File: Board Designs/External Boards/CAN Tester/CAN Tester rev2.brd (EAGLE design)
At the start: 83.8 x 100.3 mm, 30 parts, among them M1 Minifit-1, M2 Nanofit-1, M3 Nanofit-2, M4 Minifit-2, U1 ISOLATED CAN TRANSCIEVER, U3 TEENSY_3.2_SIMPLE, U4 CHARACTER_LCD

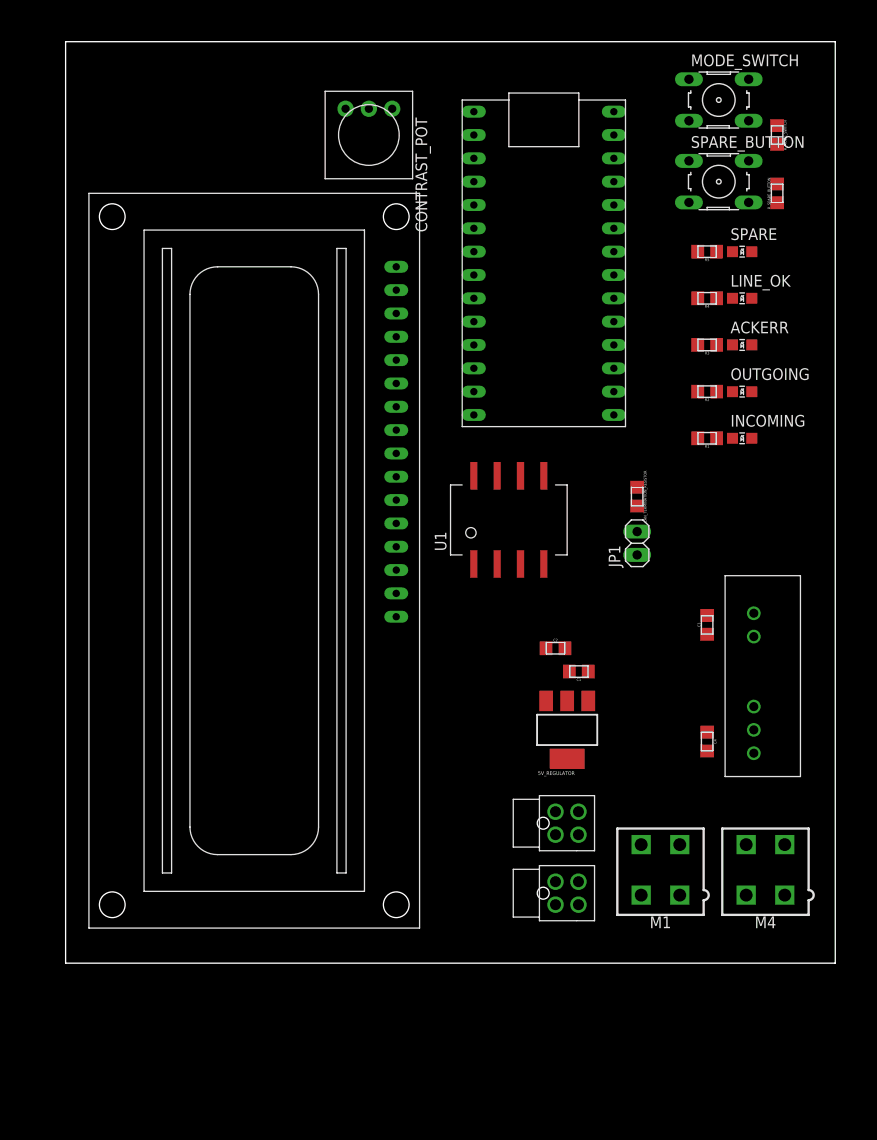
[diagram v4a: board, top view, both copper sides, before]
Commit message: Adjusted schematic to make the connections clearer for CAN_Tester, and verified it
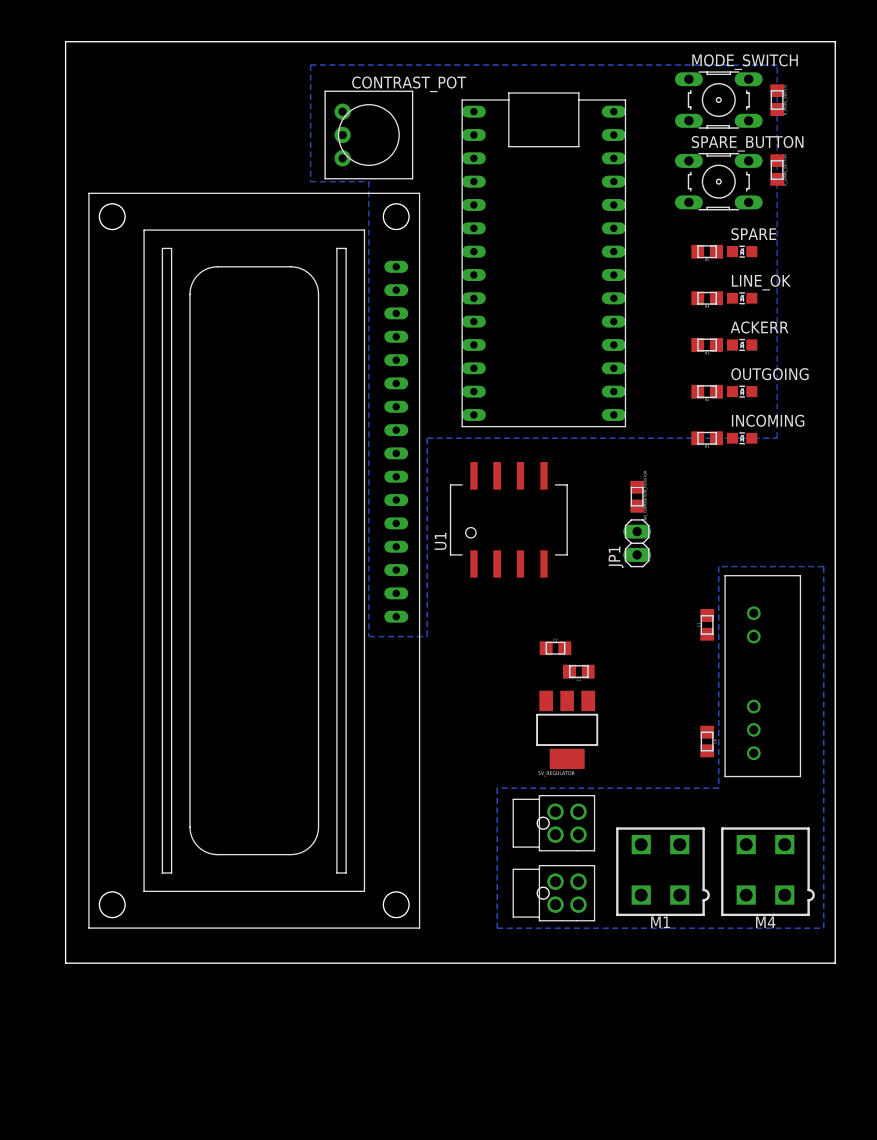
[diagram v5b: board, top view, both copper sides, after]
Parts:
- moved R_MODE_SWITCH 3.81 mm to (77.5, 92.7)
- moved R_SPARE_BUTTON 2.54 mm to (77.5, 85.1), turned to 270 degrees
- turned CONTRAST_POT to 270 degrees
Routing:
- added copper zone on layer 16, net GND
- added copper zone on layer 16, net GND_ISOLATED
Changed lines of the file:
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@@
 <param name="TopRouterVariant" value="1"/>
 <param name="tpViaShape" value="round"/>
-<param name="PrefDir.1" value="0"/>
+<param name="PrefDir.1" value="a"/>
 <param name="PrefDir.2" value="0"/>
 <param name="PrefDir.3" value="0"/>
@@
 <param name="PrefDir.14" value="0"/>
 <param name="PrefDir.15" value="0"/>
-<param name="PrefDir.16" value="a"/>
+<param name="PrefDir.16" value="0"/>
 <param name="cfVia" value="8"/>
 <param name="cfNonPref" value="5"/>
@@
 <attribute name="VALUE" x="61.5188" y="49.53" size="0.3048" layer="27" rot="R270" align="top-center"/>
 </element>
-<element name="CONTRAST_POT" library="HyTechDevices" package="TRIM-3386" value="10k" x="33.02" y="88.9" smashed="yes" rot="R180">
-<attribute name="NAME" x="38.1" y="90.805" size="1.27" layer="25" rot="R270"/>
-<attribute name="VALUE" x="26.67" y="90.805" size="1.27" layer="27" rot="R270"/>
+<element name="CONTRAST_POT" library="HyTechDevices" package="TRIM-3386" value="10k" x="33.02" y="88.9" smashed="yes" rot="R270">
+<attribute name="NAME" x="31.115" y="93.98" size="1.27" layer="25"/>
+<attribute name="VALUE" x="31.115" y="82.55" size="1.27" layer="27"/>
 </element>
 <element name="INCOMING" library="HyTechDevices" package="LED-805" value="YELLOW" x="73.66" y="55.88" smashed="yes" rot="R270">
@@
 <attribute name="VALUE" x="69.85" y="76.9112" size="0.3048" layer="27" rot="R180" align="top-center"/>
 </element>
-<element name="R_MODE_SWITCH" library="HyTechDevices" package="0805" value="10K" x="77.47" y="88.9" smashed="yes" rot="R270">
-<attribute name="NAME" x="78.1939" y="88.9" size="0.3048" layer="25" rot="R270" align="bottom-center"/>
-<attribute name="VALUE" x="76.7588" y="88.9" size="0.3048" layer="27" rot="R270" align="top-center"/>
-</element>
-<element name="R_SPARE_BUTTON" library="HyTechDevices" package="0805" value="10K" x="77.47" y="82.55" smashed="yes" rot="R90">
-<attribute name="NAME" x="76.7461" y="82.55" size="0.3048" layer="25" rot="R90" align="bottom-center"/>
-<attribute name="VALUE" x="78.1812" y="82.55" size="0.3048" layer="27" rot="R90" align="top-center"/>
+<element name="R_MODE_SWITCH" library="HyTechDevices" package="0805" value="10K" x="77.47" y="92.71" smashed="yes" rot="R270">
+<attribute name="NAME" x="78.1939" y="92.71" size="0.3048" layer="25" rot="R270" align="bottom-center"/>
+<attribute name="VALUE" x="76.7588" y="92.71" size="0.3048" layer="27" rot="R270" align="top-center"/>
+</element>
+<element name="R_SPARE_BUTTON" library="HyTechDevices" package="0805" value="10K" x="77.47" y="85.09" smashed="yes" rot="R270">
+<attribute name="NAME" x="78.1939" y="85.09" size="0.3048" layer="25" rot="R270" align="bottom-center"/>
+<attribute name="VALUE" x="76.7588" y="85.09" size="0.3048" layer="27" rot="R270" align="top-center"/>
 </element>
 <element name="SPARE" library="HyTechDevices" package="LED-805" value="WHITE" x="73.66" y="76.2" smashed="yes" rot="R270">
@@
 <contactref element="CAN_TERMINATION_RESISTOR" pad="1"/>
 <wire x1="49.53" y1="51.79" x2="62.23" y2="50.555" width="0" layer="19" extent="1-1"/>
-<wire x1="55.84" y1="15.22" x2="49.53" y2="51.79" width="0" layer="19" extent="1-1"/>
+<wire x1="55.84" y1="15.22" x2="62.23" y2="50.555" width="0" layer="19" extent="1-1"/>
 <wire x1="55.84" y1="7.6" x2="55.84" y2="15.22" width="0" layer="19" extent="1-1"/>
 <wire x1="66.87" y1="11.64" x2="55.84" y2="15.22" width="0" layer="19" extent="1-1"/>
@@
 </signal>
 <signal name="+3V3">
-<contactref element="SPARE_BUTTON" pad="2"/>
-<contactref element="SPARE_BUTTON" pad="1"/>
 <contactref element="U3" pad="3.3V"/>
-<contactref element="MODE_SWITCH" pad="1"/>
-<contactref element="MODE_SWITCH" pad="2"/>
 <contactref element="U4" pad="2"/>
 <contactref element="U4" pad="15"/>
 <contactref element="CONTRAST_POT" pad="3"/>
+<contactref element="MODE_SWITCH" pad="1"/>
+<contactref element="MODE_SWITCH" pad="2"/>
+<contactref element="SPARE_BUTTON" pad="2"/>
+<contactref element="SPARE_BUTTON" pad="1"/>
 <wire x1="67.8688" y1="94.9706" x2="74.3712" y2="94.9706" width="0" layer="19" extent="1-1"/>
 <wire x1="74.3712" y1="86.0806" x2="74.3712" y2="94.9706" width="0" layer="19" extent="1-1"/>
@@
 <wire x1="59.69" y1="86.36" x2="67.8688" y2="86.0806" width="0" layer="19" extent="1-1"/>
 <wire x1="36" y1="72.01" x2="59.69" y2="86.36" width="0" layer="19" extent="1-1"/>
-<wire x1="30.48" y1="91.7575" x2="36" y2="72.01" width="0" layer="19" extent="1-1"/>
+<wire x1="30.1625" y1="86.36" x2="36" y2="72.01" width="0" layer="19" extent="1-1"/>
 <wire x1="36" y1="38.99" x2="36" y2="72.01" width="0" layer="19" extent="1-1"/>
 </signal>
@@
 <contactref element="CONTRAST_POT" pad="2"/>
 <contactref element="U4" pad="3"/>
-<wire x1="36" y1="69.47" x2="33.02" y2="91.7575" width="0" layer="19" extent="1-1"/>
+<wire x1="36" y1="69.47" x2="30.1625" y2="88.9" width="0" layer="19" extent="1-1"/>
 </signal>
 <signal name="N$17">
@@
 <contactref element="U$1" pad="+VIN"/>
 <wire x1="69.85" y1="23.885" x2="74.93" y2="24.13" width="0" layer="19" extent="1-1"/>
-<wire x1="53.34" y1="15.22" x2="69.85" y2="23.885" width="0" layer="19" extent="1-1"/>
+<wire x1="56.91" y1="27.28" x2="69.85" y2="23.885" width="0" layer="19" extent="1-1"/>
+<wire x1="56.905" y1="30.48" x2="56.91" y2="27.28" width="0" layer="19" extent="1-1"/>
+<wire x1="53.34" y1="15.22" x2="56.91" y2="27.28" width="0" layer="19" extent="1-1"/>
 <wire x1="53.34" y1="7.6" x2="53.34" y2="15.22" width="0" layer="19" extent="1-1"/>
 <wire x1="66.87" y1="6.14" x2="53.34" y2="7.6" width="0" layer="19" extent="1-1"/>
 <wire x1="78.3" y1="6.14" x2="66.87" y2="6.14" width="0" layer="19" extent="1-1"/>
-<wire x1="56.91" y1="27.28" x2="53.34" y2="15.22" width="0" layer="19" extent="1-1"/>
-<wire x1="56.905" y1="30.48" x2="56.91" y2="27.28" width="0" layer="19" extent="1-1"/>
 </signal>
 <signal name="N$12">
 <contactref element="MODE_SWITCH" pad="4"/>
 <contactref element="R_MODE_SWITCH" pad="1"/>
-<wire x1="74.3712" y1="90.4494" x2="77.47" y2="89.925" width="0" layer="19" extent="1-1"/>
+<wire x1="74.3712" y1="90.4494" x2="77.47" y2="93.735" width="0" layer="19" extent="1-1"/>
 </signal>
 <signal name="N$14">
 <contactref element="SPARE_BUTTON" pad="4"/>
 <contactref element="R_SPARE_BUTTON" pad="1"/>
-<wire x1="74.3712" y1="81.5594" x2="77.47" y2="81.525" width="0" layer="19" extent="1-1"/>
+<wire x1="74.3712" y1="81.5594" x2="77.47" y2="86.115" width="0" layer="19" extent="1-1"/>
 </signal>
 <signal name="N$15">
@@
 <contactref element="U4" pad="1"/>
 <contactref element="U1" pad="P$4"/>
-<wire x1="77.47" y1="83.575" x2="77.47" y2="87.875" width="0" layer="19" extent="1-1"/>
-<wire x1="74.71" y1="76.2" x2="77.47" y2="83.575" width="0" layer="19" extent="1-1"/>
+<polygon width="0.127" layer="16">
+<vertex x="26.67" y="96.52"/>
+<vertex x="26.67" y="83.82"/>
+<vertex x="33.02" y="83.82"/>
+<vertex x="33.02" y="34.29"/>
+<vertex x="39.37" y="34.29"/>
+<vertex x="39.37" y="55.88"/>
+<vertex x="77.47" y="55.88"/>
+<vertex x="77.47" y="96.52"/>
+</polygon>
+<wire x1="77.47" y1="84.065" x2="77.47" y2="91.685" width="0" layer="19" extent="1-1"/>
+<wire x1="74.71" y1="76.2" x2="77.47" y2="84.065" width="0" layer="19" extent="1-1"/>
 <wire x1="74.71" y1="71.12" x2="74.71" y2="76.2" width="0" layer="19" extent="1-1"/>
 <wire x1="74.71" y1="66.04" x2="74.71" y2="71.12" width="0" layer="19" extent="1-1"/>
@@
 <wire x1="74.93" y1="36.83" x2="74.71" y2="55.88" width="0" layer="19" extent="1-1"/>
 <wire x1="69.85" y1="36.585" x2="74.93" y2="36.83" width="0" layer="19" extent="1-1"/>
-<wire x1="52.07" y1="42.19" x2="36" y2="36.45" width="0" layer="19" extent="1-1"/>
+<wire x1="52.07" y1="42.19" x2="69.85" y2="36.585" width="0" layer="19" extent="1-1"/>
+<wire x1="36" y1="36.45" x2="52.07" y2="42.19" width="0" layer="19" extent="1-1"/>
 </signal>
 <signal name="+5V">
@@
 <contactref element="M2" pad="P$2"/>
 <contactref element="M1" pad="2"/>
+<polygon width="0.127" layer="16">
+<vertex x="46.99" y="2.54"/>
+<vertex x="82.55" y="2.54"/>
+<vertex x="82.55" y="41.91"/>
+<vertex x="71.12" y="41.91"/>
+<vertex x="71.12" y="17.78"/>
+<vertex x="46.99" y="17.78"/>
+</polygon>
+<contactref element="U1" pad="P$5"/>
 <contactref element="5V_REGULATOR" pad="2"/>
 <contactref element="5V_REGULATOR" pad="4"/>
 <contactref element="C1" pad="2"/>
 <contactref element="C2" pad="2"/>
-<contactref element="U1" pad="P$5"/>
 <wire x1="54.365" y1="33.02" x2="52.07" y2="51.79" width="0" layer="19" extent="1-1"/>
 <wire x1="54.855" y1="30.48" x2="54.365" y2="33.02" width="0" layer="19" extent="1-1"/>
@@
 <wire x1="54.61" y1="20.98" x2="54.61" y2="27.28" width="0" layer="19" extent="1-1"/>
 <wire x1="53.34" y1="12.72" x2="54.61" y2="20.98" width="0" layer="19" extent="1-1"/>
-<wire x1="53.34" y1="5.1" x2="53.34" y2="12.72" width="0" layer="19" extent="1-1"/>
-<wire x1="62.67" y1="6.14" x2="53.34" y2="5.1" width="0" layer="19" extent="1-1"/>
-<wire x1="74.1" y1="6.14" x2="62.67" y2="6.14" width="0" layer="19" extent="1-1"/>
-<wire x1="74.93" y1="21.59" x2="74.1" y2="6.14" width="0" layer="19" extent="1-1"/>
 <wire x1="69.85" y1="21.835" x2="74.93" y2="21.59" width="0" layer="19" extent="1-1"/>
 </signal>

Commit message: Working on board layout
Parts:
- moved INCOMING 10.2 mm to (73.7, 45.7)
- moved R1 10.2 mm to (69.8, 45.7)
- moved OUTGOING 7.62 mm to (73.7, 53.3)
- moved R2 7.62 mm to (69.8, 53.3)
- moved ACKERR 5.08 mm to (73.7, 61.0)
- moved R3 5.08 mm to (69.8, 61.0)
- moved LINE_OK 2.54 mm to (73.7, 68.6)
- moved R4 2.54 mm to (69.8, 68.6)
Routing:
- net +3V3: track 0.00 -> 171.1 mm
- net CANH: track 0.00 -> 163.2 mm
- net +5V_ISOLATED: track 0.00 -> 154.3 mm
- net GND_ISOLATED: track 0.00 -> 134.4 mm, vias 0 -> 2
- net CANL: track 0.00 -> 99.9 mm
- net +12V: track 0.00 -> 56.6 mm
- net GND: track 0.00 -> 42.6 mm
- net N$13: track 0.00 -> 38.2 mm
- net N$22: track 0.00 -> 34.3 mm
- net N$21: track 0.00 -> 29.6 mm
- net N$20: track 0.00 -> 29.1 mm
- net +5V: track 0.00 -> 27.8 mm
- net N$19: track 0.00 -> 26.1 mm
- net VO: track 0.00 -> 26.0 mm
- net N$18: track 0.00 -> 17.8 mm
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
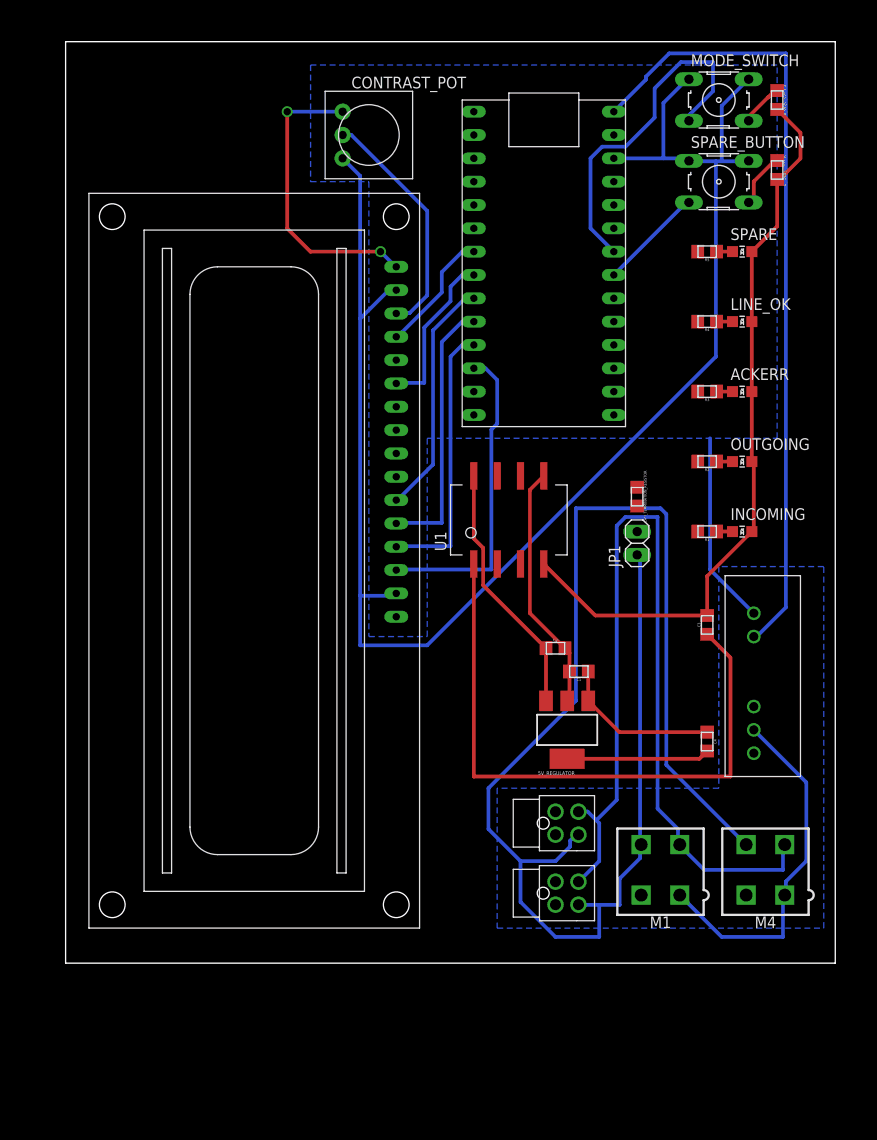
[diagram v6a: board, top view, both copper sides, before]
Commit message: Finished CAN_Tester v2 board
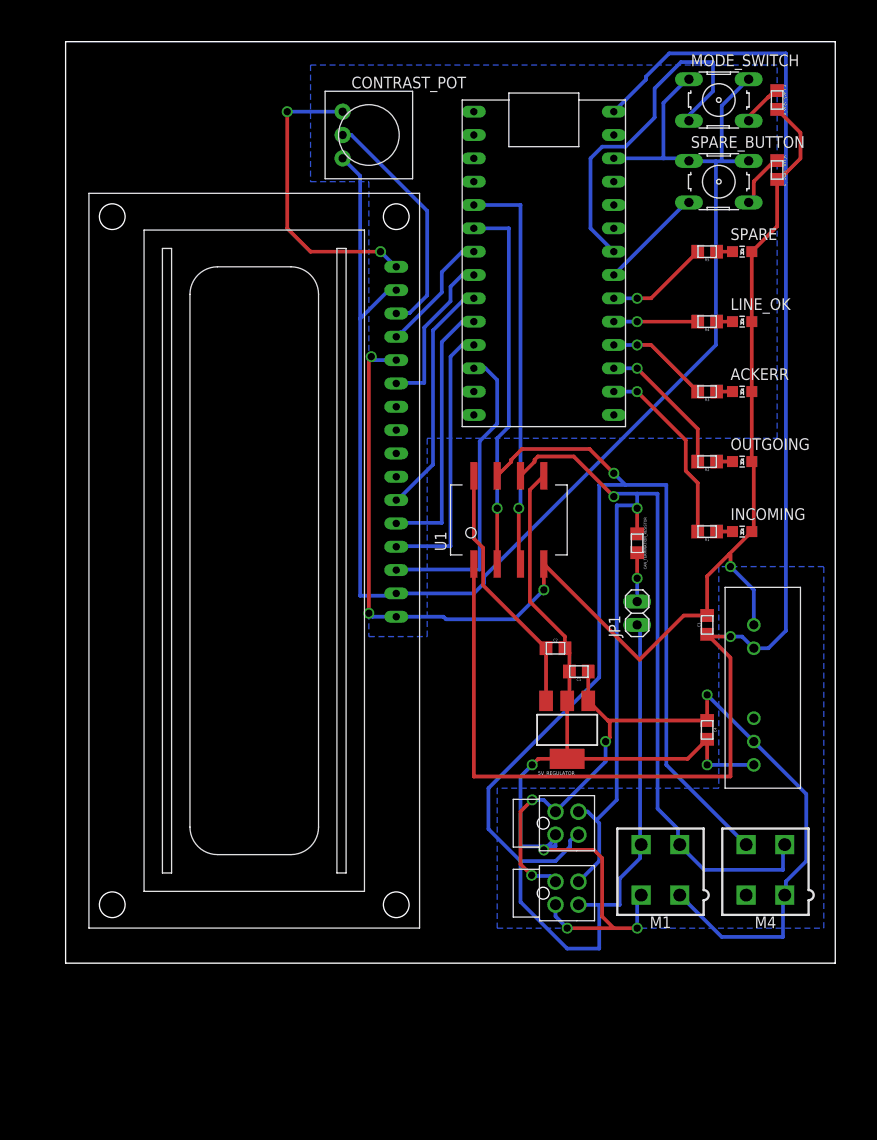
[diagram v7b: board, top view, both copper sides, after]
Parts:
- moved JP1 7.62 mm to (62.2, 36.8)
- moved CAN_TERMINATION_RESISTOR 5.08 mm to (62.2, 44.5)
- moved C4 1.27 mm to (69.8, 24.1)
- moved U$1 1.27 mm to (74.9, 29.2)
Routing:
- net GND: track 42.6 -> 107.0 mm, vias 0 -> 5
- net GND_ISOLATED: track 134.4 -> 180.6 mm, vias 2 -> 6
- net CANTX: track 0.00 -> 44.3 mm, vias 0 -> 1
- net CANRX: track 0.00 -> 40.9 mm, vias 0 -> 1
- net +12V: track 56.6 -> 92.6 mm, vias 0 -> 4
- net CANL: track 99.9 -> 124.3 mm, vias 0 -> 2
- net N$1: track 0.00 -> 20.5 mm, vias 0 -> 1
- net N$4: track 0.00 -> 15.4 mm, vias 0 -> 1
- net CANH: track 163.2 -> 178.3 mm, vias 0 -> 1
- net +3V3: track 171.1 -> 159.1 mm
- net N$5: track 0.00 -> 11.2 mm, vias 0 -> 1
- net N$7: track 0.00 -> 11.2 mm, vias 0 -> 1
- net N$6: track 0.00 -> 9.14 mm, vias 0 -> 1
- net +5V_ISOLATED: track 154.3 -> 162.0 mm, vias 0 -> 1
- net N$15: track 0.00 -> 5.32 mm, vias 0 -> 1
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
